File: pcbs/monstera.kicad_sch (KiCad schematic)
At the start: 0 parts

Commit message: Add custom symbol library, and make symbols for esp32-s3 supermini and ld2410c
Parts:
- added U1: ESP32-S3 Supermini, symbol Monstera lib:ESP32-S3_Supermini
- added U2: LD2410C, symbol Monstera lib:LD2410C
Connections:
- new net +3V3: U1.16 (3V3)
- new net +5V: U1.18 (5V), U2.5 (VCC)
- new net GND: U1.17 (GND), U2.4 (GND)
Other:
- note added: "5v input required, not 3v3"

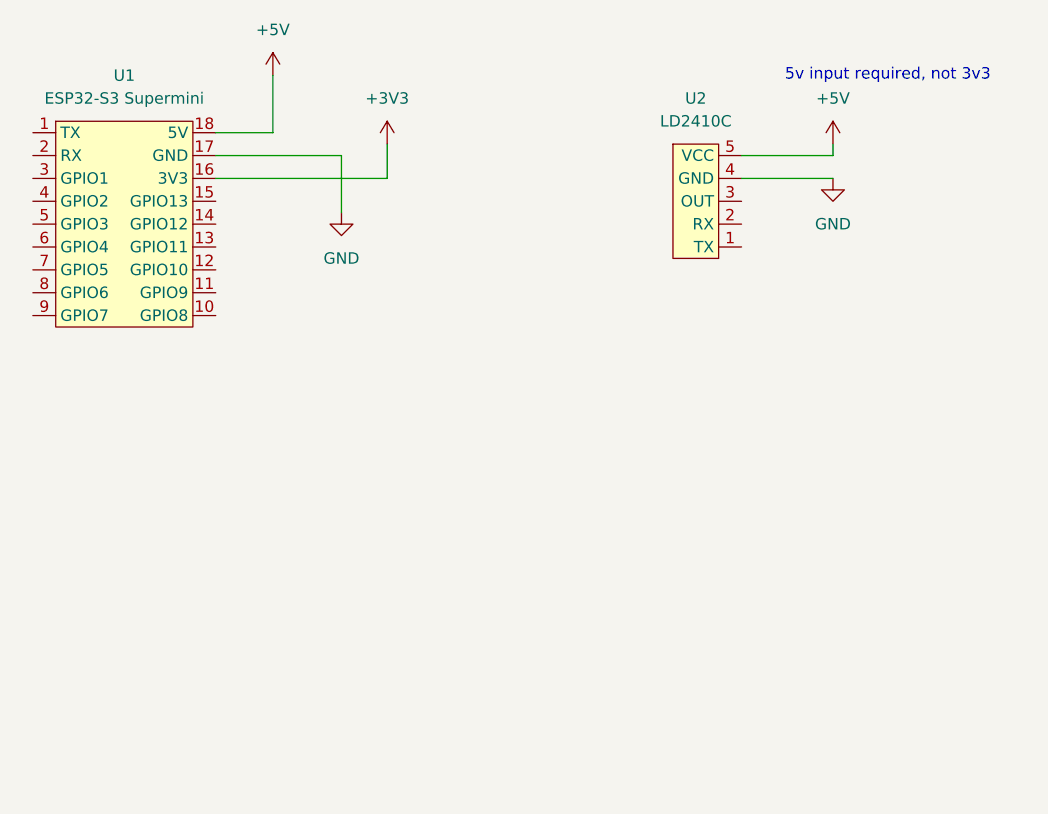
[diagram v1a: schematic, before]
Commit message: Update PCBs to include i2c connector
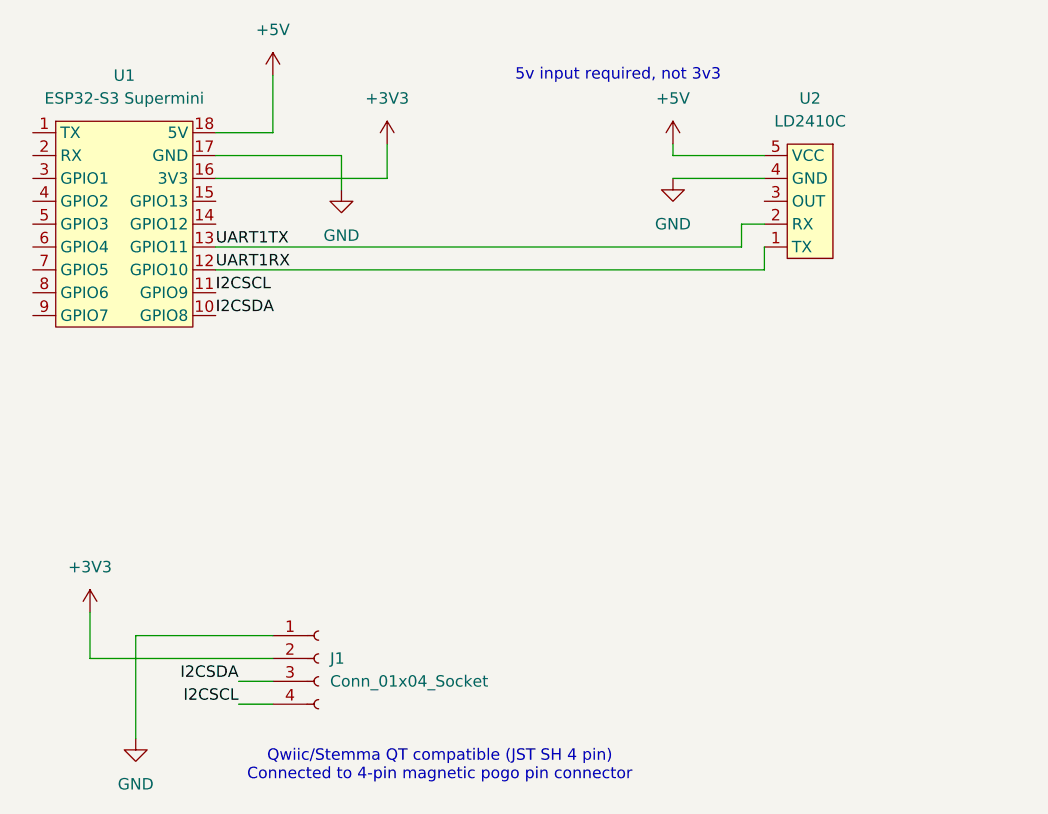
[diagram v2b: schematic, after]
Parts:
- added J1: Conn_01x04_Socket, symbol Connector:Conn_01x04_Socket
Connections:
- net +3V3: now also J1.2 (Pin_2)
- net GND: now also J1.1 (Pin_1)
- net I2CSDA: now reaches U1.10 (GPIO8)
- net I2CSDA: now also J1.3 (Pin_3)
- net I2CSCL: now reaches U1.11 (GPIO9)
- net I2CSCL: now also J1.4 (Pin_4)
- net UART1RX: now reaches U1.12 (GPIO10)
- net UART1RX: now also U2.1 (TX)
- net UART1TX: now reaches U1.13 (GPIO11)
- net UART1TX: now also U2.2 (RX)
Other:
- note added: "Qwiic/Stemma QT compatible (JST SH 4 pin) Connected to 4-pin magnetic pogo pin connector"
- moved on the sheet: U2

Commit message: kicad: add simple hall effect, reed, and bme680 sensors
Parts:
- added J3, J6, J7: Conn_01x03_Socket, symbol Connector:Conn_01x03_Socket
- added J4, J5: Conn_01x04_Socket, symbol Connector:Conn_01x04_Socket
- added R1, R2: R_Small, symbol Device:R_Small
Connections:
- net +3V3: now also J3.2 (Pin_2), J4.2 (Pin_2), J5.2 (Pin_2), J6.2 (Pin_2), J7.2 (Pin_2), R1.1, R2.1
- net GND: now also J3.1 (Pin_1), J4.1 (Pin_1), J5.1 (Pin_1), J6.1 (Pin_1), J7.1 (Pin_1)
- net I2CSCL: now also J4.4 (Pin_4), J5.4 (Pin_4), R1.2
- net I2CSDA: now also J4.3 (Pin_3), J5.3 (Pin_3), R2.2
- net at U1.3 (GPIO1): now also J3.3 (Pin_3)
- net at U1.4 (GPIO2): now also J6.3 (Pin_3)
- net at U1.6 (GPIO4): now also J7.3 (Pin_3)
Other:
- note added: "JST PH 2mm 3-pin, compatible with STEMMA. Used for digital, analog, pwm, whatever with 1 signal pin"
- note added: "Qwiic/Stemma QT compatible (JST SH 4 pin, or maybe PH 4 pin???)"
- note added: "exact number unknown"
- note removed: "Qwiic/Stemma QT compatible (JST SH 4 pin) Connected to 4-pin magnetic pogo pin connector"
- moved on the sheet: J1, U1, U2

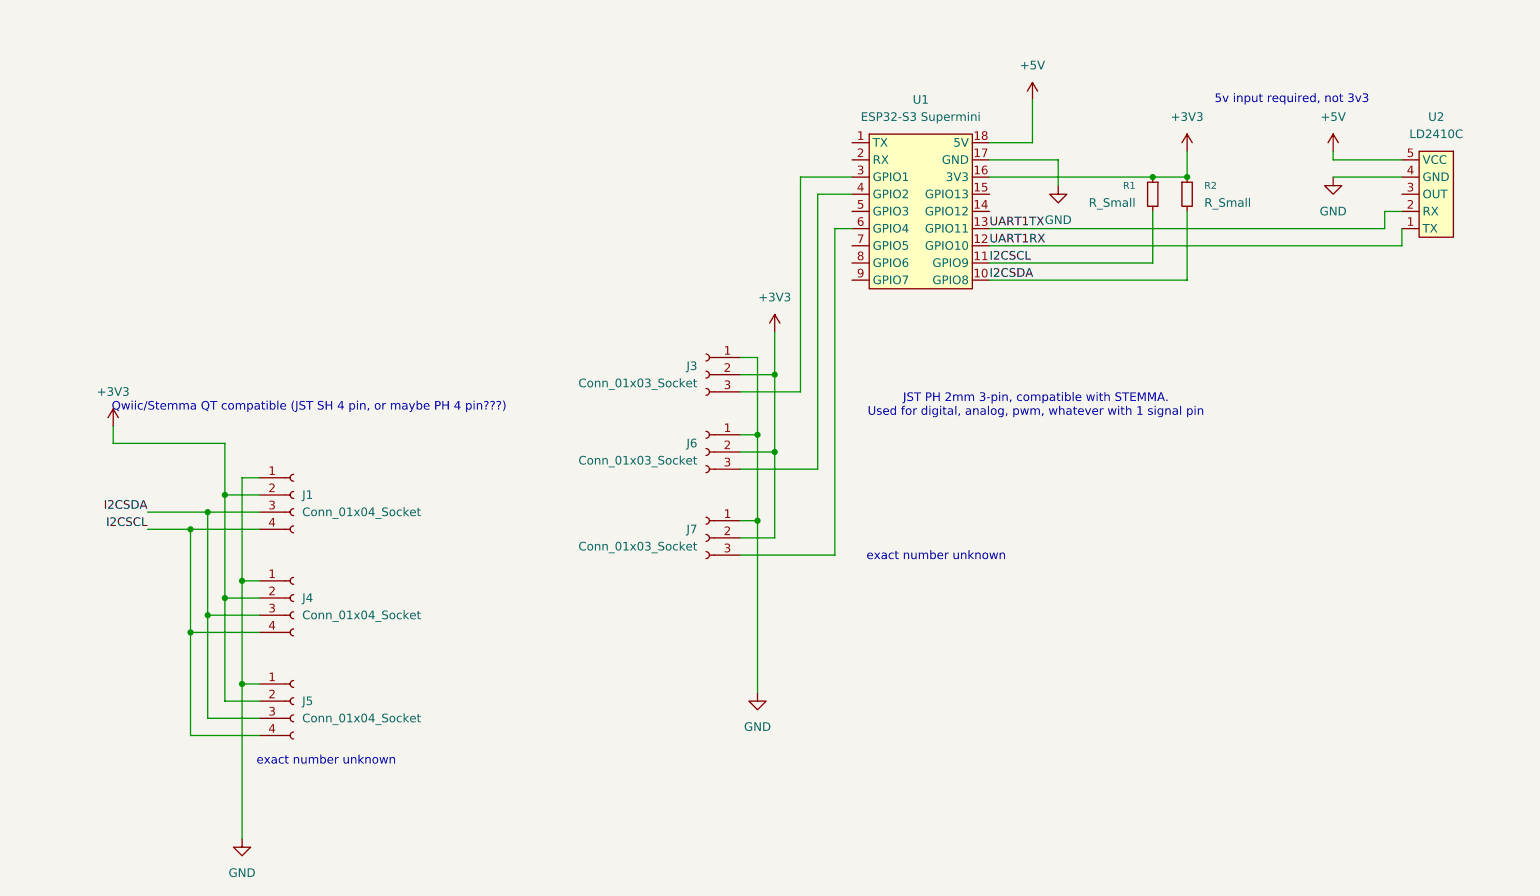
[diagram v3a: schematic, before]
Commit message: add ld2450, recreate simple hall effect sensor, add ssd1306 display
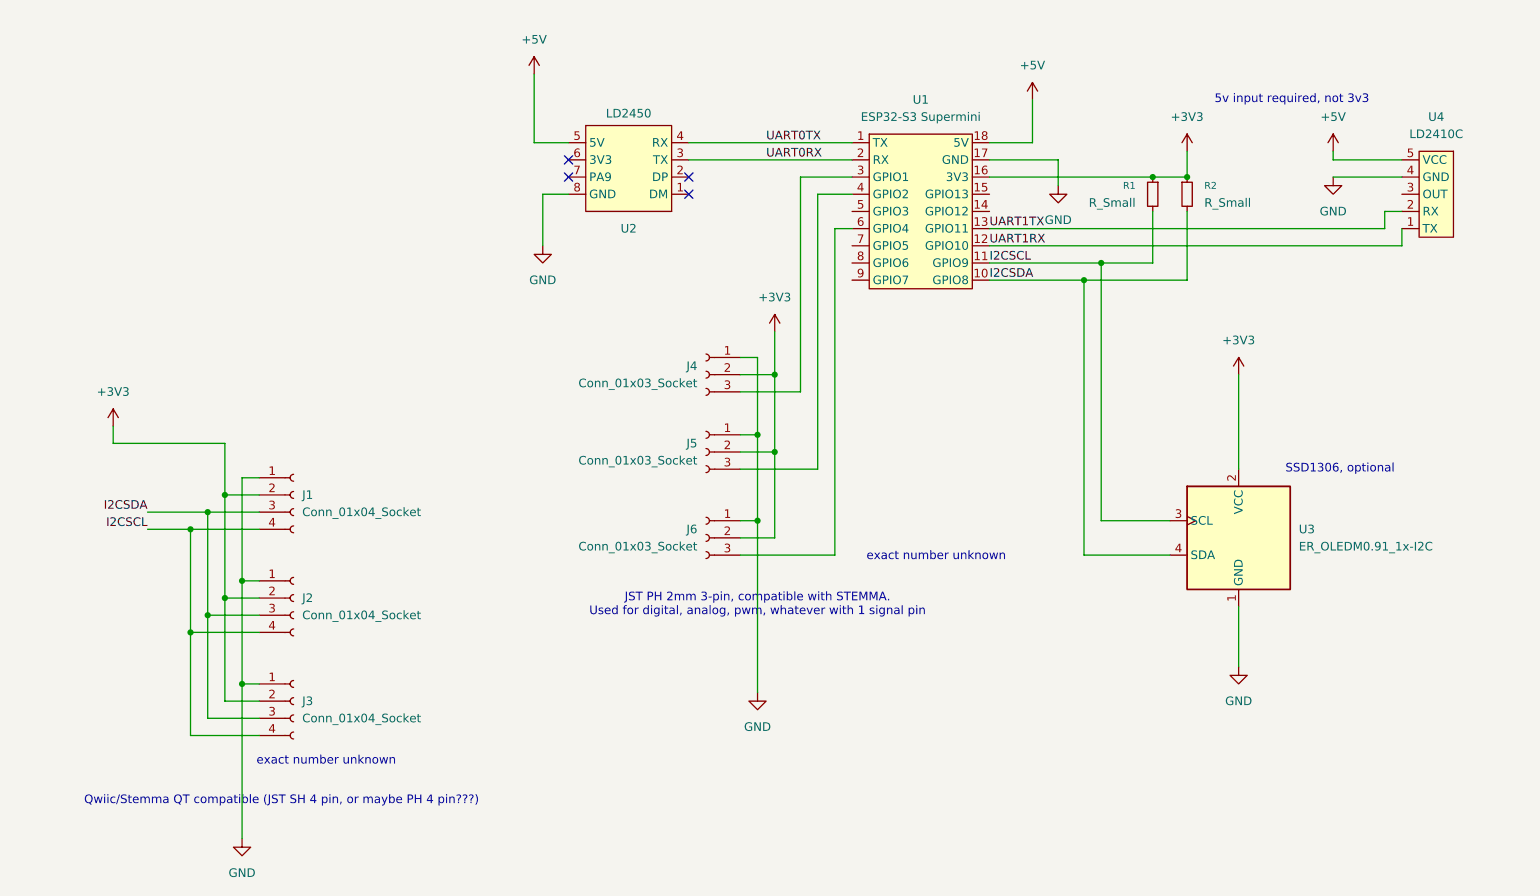
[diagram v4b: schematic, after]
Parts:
- added U2: LD2450, ld2450:ld2450, symbol ld2450:ld2450
- added U3: ER_OLEDM0.91_1x-I2C, Connector_PinHeader_2.54mm:PinHeader_1x04_P2.54mm_Vertical, symbol Display_Graphic:ER_OLEDM0.91_1x-I2C
- renumbered J4 to J2, J5 to J3, J3 to J4, J6 to J5, J7 to J6, U2 to U4
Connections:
- net +3V3: now also U3.2 (VCC)
- net +5V: now also U2.5 (5V)
- net GND: now also U2.8 (GND), U3.1 (GND)
- net I2CSCL: now also U3.3 (SCL)
- net I2CSDA: now also U3.4 (SDA)
- net UART0TX: now reaches U1.1 (TX)
- net UART0TX: now also U2.4 (RX)
- net UART0RX: now reaches U1.2 (RX)
- net UART0RX: now also U2.3 (TX)
- no-connect marks 0 -> 4
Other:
- note added: "SSD1306, optional"

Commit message: create aloe repo and submodule for easier library reuse
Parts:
- U1: symbol Monstera lib:ESP32-S3_Supermini -> Aloe:ESP32-S3_Supermini
- U4: symbol Monstera lib:LD2410C -> Aloe:LD2410C
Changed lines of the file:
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@@
 	)
 	(symbol
-		(lib_id "Monstera lib:ESP32-S3_Supermini")
+		(lib_id "Aloe:ESP32-S3_Supermini")
 		(at 185.42 80.01 0)
 		(unit 1)
@@
 	)
 	(symbol
-		(lib_id "Monstera lib:LD2410C")
+		(lib_id "Aloe:LD2410C")
 		(at 260.35 66.04 0)
 		(mirror y)
@@
 		(fields_autoplaced yes)
 		(property "Reference" "U4"
-			(at 260.35 54.61 0)
+			(at 264.16 64.7699 0)
 			(show_name no)
 			(do_not_autoplace no)
@@
 					(size 1.27 1.27)
 				)
+				(justify right)
 			)
 		)
 		(property "Value" "LD2410C"
-			(at 260.35 57.15 0)
+			(at 264.16 67.3099 0)
 			(show_name no)
 			(do_not_autoplace no)
@@
 					(size 1.27 1.27)
 				)
+				(justify right)
 			)
 		)

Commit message: Initial PCB layout
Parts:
- J1, J2, J3: footprint (none) -> Connector_JST:JST_PH_S4B-PH-K_1x04_P2.00mm_Horizontal
- J4, J5, J6: footprint (none) -> Connector_JST:JST_PH_S3B-PH-K_1x03_P2.00mm_Horizontal
- R1, R2: value R_Small -> 1k; footprint (none) -> Resistor_SMD:R_0805_2012Metric_Pad1.20x1.40mm_HandSolder
- U1: footprint (none) -> Aloe:ESP32-S3 Supermini
- U2: footprint ld2450:ld2450 -> LD2450:ld2450
- U3: footprint Connector_PinHeader_2.54mm:PinHeader_1x04_P2.54mm_Vertical -> Aloe:SSD1306_1.3
- U4: footprint (none) -> Aloe:ld2410c
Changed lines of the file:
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@@
 			)
 		)
-		(property "Footprint" ""
+		(property "Footprint" "Connector_JST:JST_PH_S3B-PH-K_1x03_P2.00mm_Horizontal"
 			(at 152.4 104.14 0)
 			(hide yes)
@@
 			)
 		)
-		(property "Footprint" ""
+		(property "Footprint" "Connector_JST:JST_PH_S4B-PH-K_1x04_P2.00mm_Horizontal"
 			(at 91.44 140.97 0)
 			(hide yes)
@@
 			)
 		)
-		(property "Value" "R_Small"
+		(property "Value" "1k"
 			(at 215.9 67.3099 0)
 			(show_name no)
@@
 			)
 		)
-		(property "Footprint" ""
+		(property "Footprint" "Resistor_SMD:R_0805_2012Metric_Pad1.20x1.40mm_HandSolder"
 			(at 218.44 66.04 0)
 			(hide yes)
@@
 			)
 		)
-		(property "Value" "R_Small"
+		(property "Value" "1k"
 			(at 226.06 67.3099 0)
 			(show_name no)
@@
 			)
 		)
-		(property "Footprint" ""
+		(property "Footprint" "Resistor_SMD:R_0805_2012Metric_Pad1.20x1.40mm_HandSolder"
 			(at 223.52 66.04 0)
 			(hide yes)
@@
 			)
 		)
-		(property "Footprint" ""
+		(property "Footprint" "Connector_JST:JST_PH_S4B-PH-K_1x04_P2.00mm_Horizontal"
 			(at 91.44 125.73 0)
 			(hide yes)
@@
 			)
 		)
-		(property "Footprint" ""
+		(property "Footprint" "Connector_JST:JST_PH_S3B-PH-K_1x03_P2.00mm_Horizontal"
 			(at 152.4 92.71 0)
 			(hide yes)
@@
 			)
 		)
-		(property "Footprint" ""
+		(property "Footprint" "Connector_JST:JST_PH_S4B-PH-K_1x04_P2.00mm_Horizontal"
 			(at 91.44 110.49 0)
 			(hide yes)
@@
 			)
 		)
-		(property "Footprint" ""
+		(property "Footprint" "Connector_JST:JST_PH_S3B-PH-K_1x03_P2.00mm_Horizontal"
 			(at 152.4 116.84 0)
 			(hide yes)
@@
 			)
 		)
-		(property "Footprint" ""
+		(property "Footprint" "Aloe:ESP32-S3 Supermini"
 			(at 185.42 58.42 0)
 			(hide yes)
@@
 			)
 		)
-		(property "Footprint" ""
+		(property "Footprint" "Aloe:ld2410c"
 			(at 260.35 66.04 0)
 			(hide yes)
@@
 			)
 		)
-		(property "Footprint" "ld2450:ld2450"
+		(property "Footprint" "LD2450:ld2450"
 			(at 140.97 53.34 0)
 			(hide yes)
@@
 			)
 		)
-		(property "Footprint" "Connector_PinHeader_2.54mm:PinHeader_1x04_P2.54mm_Vertical"
+		(property "Footprint" "Aloe:SSD1306_1.3"
 			(at 249.174 129.54 0)
 			(hide yes)

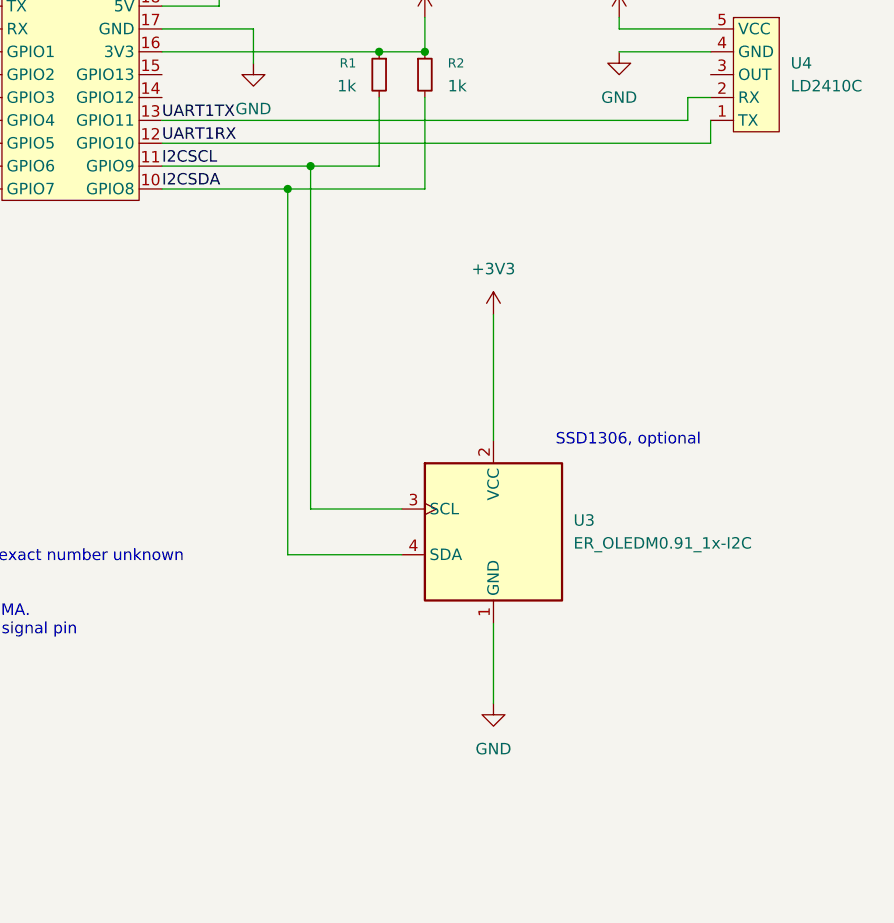
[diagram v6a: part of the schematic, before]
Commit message: pcb: remove OLED display
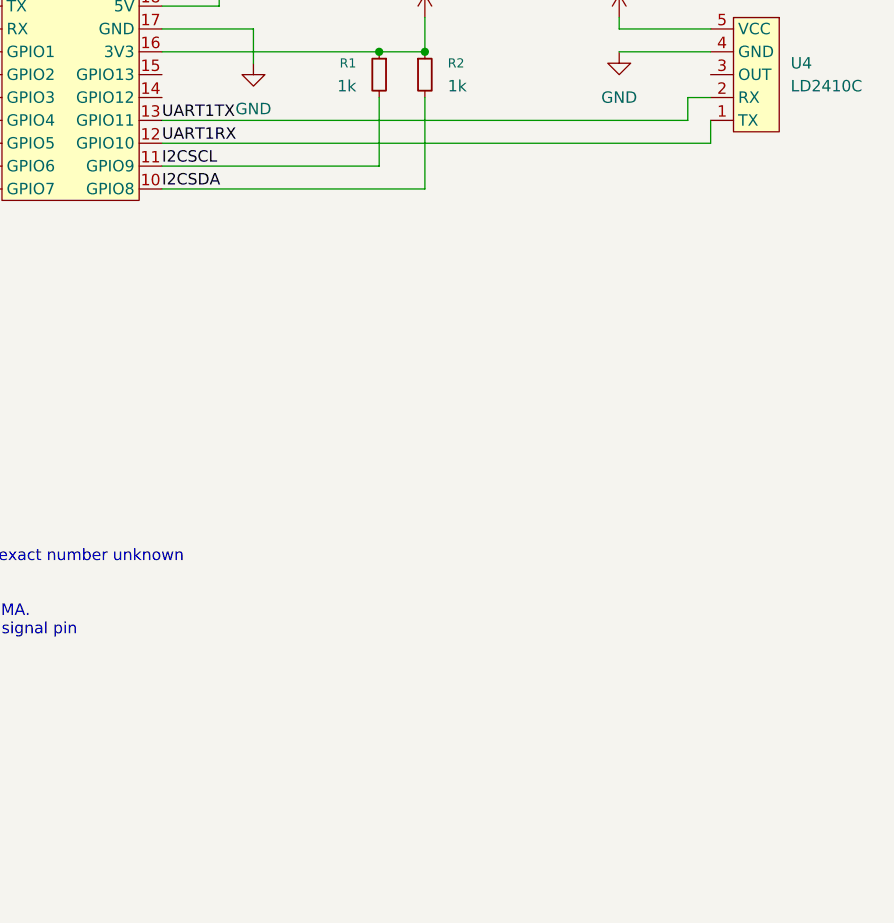
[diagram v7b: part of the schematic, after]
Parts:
- removed U3: ER_OLEDM0.91_1x-I2C, Aloe:SSD1306_1.3, symbol Display_Graphic:ER_OLEDM0.91_1x-I2C
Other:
- note removed: "SSD1306, optional"
